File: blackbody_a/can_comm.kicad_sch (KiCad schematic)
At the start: 4 parts, among them J1 Conn_01x04_Pin, U1 TSL25911FN

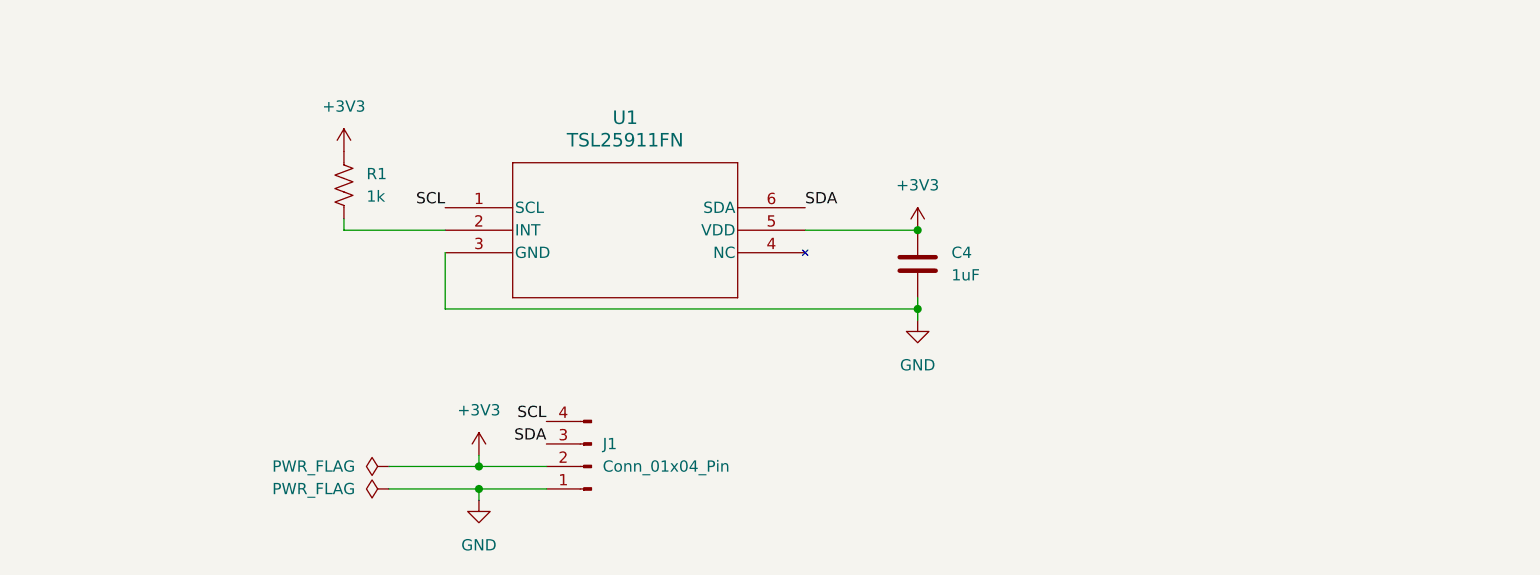
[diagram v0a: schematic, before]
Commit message: Added controller and CAN
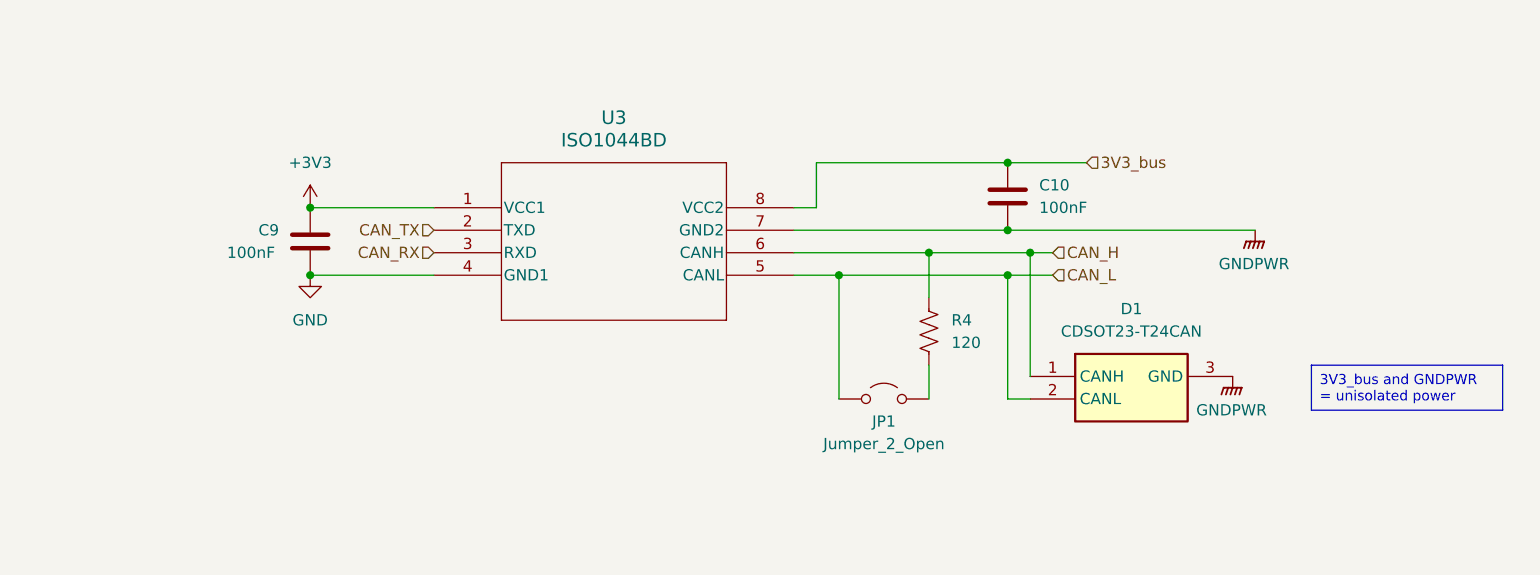
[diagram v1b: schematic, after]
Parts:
- removed C4: 1uF, symbol Device:C
- removed J1: Conn_01x04_Pin, symbol Connector:Conn_01x04_Pin
- removed R1: 1k, symbol Device:R_US
- removed U1: TSL25911FN, SON-06-FN_2000X2400_AMS, symbol TSL25911:TSL25911FN
- added C10, C9: 100nF, symbol Device:C
- added D1: CDSOT23-T24CAN, SOT95P230X117-3N, symbol CDSOT23-T24CAN:CDSOT23-T24CAN
- added JP1: Jumper_2_Open, symbol Jumper:Jumper_2_Open
- added R4: 120, symbol Device:R_US
- added U3: ISO1044BD, SOIC8_D_TEX, symbol ISO1044:ISO1044BD
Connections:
- net +3V3: now also C9.1, U3.1 (VCC1)
- net GND: now also C9.2, U3.4 (GND1)
- new net: JP1.2 (B), R4.2
- new net 3V3_bus: C10.1, U3.8 (VCC2)
- new net CAN_H: D1.1 (CANH), R4.1, U3.6 (CANH)
- new net CAN_L: D1.2 (CANL), JP1.1 (A), U3.5 (CANL)
- new net CAN_RX: U3.3 (RXD)
- new net CAN_TX: U3.2 (TXD)
- new net GNDPWR: C10.2, D1.3 (GND), U3.7 (GND2)

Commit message: Added power distribution
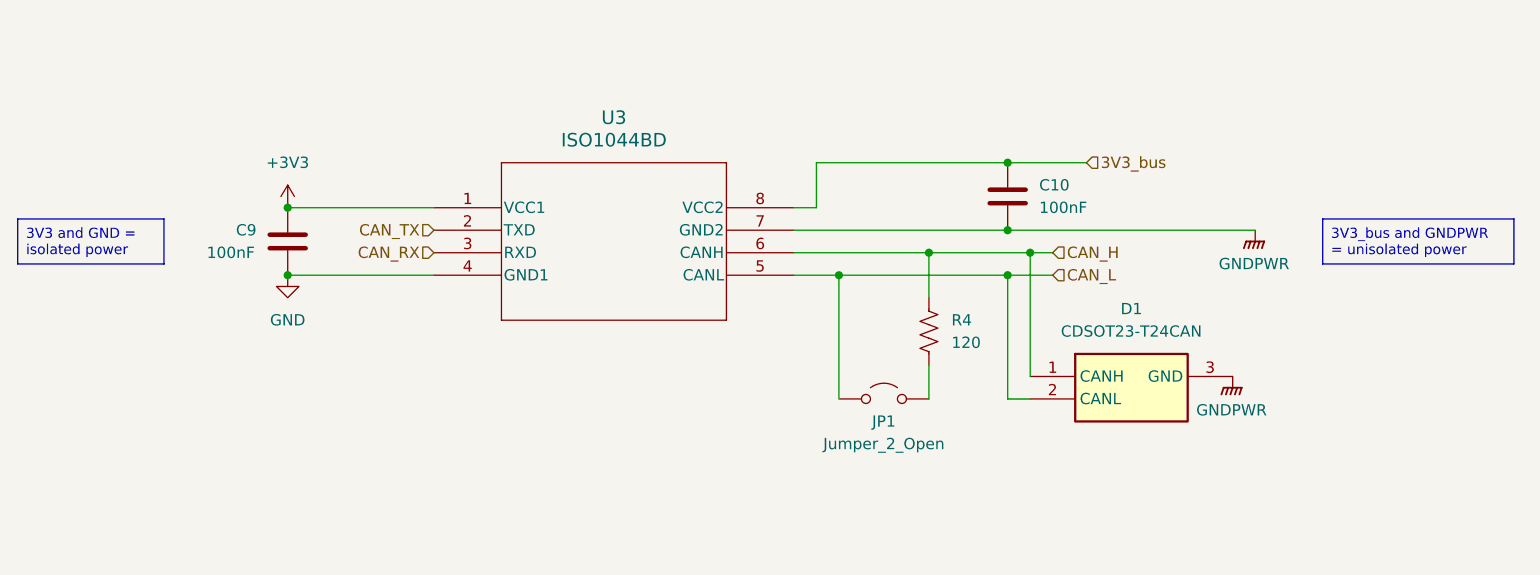
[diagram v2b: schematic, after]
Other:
- moved on the sheet: C9
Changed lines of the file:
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@@
 	(paper "A4")
 	(junction
-		(at 83.82 87.63)
+		(at 81.28 87.63)
 		(diameter 0)
 		(color 0 0 0 0)
@@
 	)
 	(junction
-		(at 83.82 95.25)
+		(at 81.28 95.25)
 		(diameter 0)
 		(color 0 0 0 0)
@@
 	(wire
 		(pts
-			(xy 83.82 95.25) (xy 97.79 95.25)
+			(xy 81.28 95.25) (xy 97.79 95.25)
 		)
 		(stroke
@@
 	(wire
 		(pts
-			(xy 97.79 87.63) (xy 83.82 87.63)
+			(xy 97.79 87.63) (xy 81.28 87.63)
 		)
 		(stroke
@@
 	(text_box "3V3_bus and GNDPWR = unisolated power"
 		(exclude_from_sim no)
-		(at 196.85 105.41 0)
+		(at 198.12 88.9 0)
 		(size 21.59 5.08)
+		(stroke
+			(width 0)
+			(type default)
+		)
+		(fill
+			(type none)
+		)
+		(effects
+			(font
+				(size 1.143 1.143)
+			)
+			(justify left top)
+		)
+	)
+	(text_box "3V3 and GND = isolated power"
+		(exclude_from_sim no)
+		(at 50.8 88.9 0)
+		(size 16.51 5.08)
 		(stroke
 			(width 0)
@@
 		)
 		(instances
-			(project ""
+			(project "blackbody_a"
 				(path "/1fc8ae43-742a-46b6-a93b-79253d0d0202/faa728f8-ddc6-4e3f-b104-4874b0828b62"
 					(reference "#PWR019")
@@
 		)
 		(instances
-			(project ""
+			(project "blackbody_a"
 				(path "/1fc8ae43-742a-46b6-a93b-79253d0d0202/faa728f8-ddc6-4e3f-b104-4874b0828b62"
 					(reference "JP1")
@@
 		)
 		(instances
-			(project ""
+			(project "blackbody_a"
 				(path "/1fc8ae43-742a-46b6-a93b-79253d0d0202/faa728f8-ddc6-4e3f-b104-4874b0828b62"
 					(reference "D1")
@@
 		)
 		(instances
-			(project ""
+			(project "blackbody_a"
 				(path "/1fc8ae43-742a-46b6-a93b-79253d0d0202/faa728f8-ddc6-4e3f-b104-4874b0828b62"
 					(reference "U3")
@@
 		)
 		(instances
-			(project ""
+			(project "blackbody_a"
 				(path "/1fc8ae43-742a-46b6-a93b-79253d0d0202/faa728f8-ddc6-4e3f-b104-4874b0828b62"
 					(reference "R4")
@@
 	(symbol
 		(lib_id "power:GND")
-		(at 83.82 95.25 0)
+		(at 81.28 95.25 0)
 		(unit 1)
 		(exclude_from_sim no)
@@
 		(fields_autoplaced yes)
 		(property "Reference" "#PWR018"
-			(at 83.82 101.6 0)
+			(at 81.28 101.6 0)
 			(effects
 				(font
@@
 		)
 		(property "Value" "GND"
-			(at 83.82 100.33 0)
+			(at 81.28 100.33 0)
 			(effects
 				(font
@@
 		)
 		(property "Footprint" ""
-			(at 83.82 95.25 0)
+			(at 81.28 95.25 0)
 			(effects
 				(font
@@
 		)
 		(property "Datasheet" ""
-			(at 83.82 95.25 0)
+			(at 81.28 95.25 0)
 			(effects
 				(font
@@
 		)
 		(property "Description" "Power symbol creates a global label with name \"GND\" , ground"
-			(at 83.82 95.25 0)
+			(at 81.28 95.25 0)
 			(effects
 				(font
@@
 		)
 		(instances
-			(project ""
+			(project "blackbody_a"
 				(path "/1fc8ae43-742a-46b6-a93b-79253d0d0202/faa728f8-ddc6-4e3f-b104-4874b0828b62"
 					(reference "#PWR018")
@@
 	(symbol
 		(lib_id "power:+3V3")
-		(at 83.82 87.63 0)
+		(at 81.28 87.63 0)
 		(unit 1)
 		(exclude_from_sim no)
@@
 		(fields_autoplaced yes)
 		(property "Reference" "#PWR017"
-			(at 83.82 91.44 0)
+			(at 81.28 91.44 0)
 			(effects
 				(font
@@
 		)
 		(property "Value" "+3V3"
-			(at 83.82 82.55 0)
+			(at 81.28 82.55 0)
 			(effects
 				(font
@@
 		)
 		(property "Footprint" ""
-			(at 83.82 87.63 0)
+			(at 81.28 87.63 0)
 			(effects
 				(font
@@
 		)
 		(property "Datasheet" ""
-			(at 83.82 87.63 0)
+			(at 81.28 87.63 0)
 			(effects
 				(font
@@
 		)
 		(property "Description" "Power symbol creates a global label with name \"+3V3\""
-			(at 83.82 87.63 0)
+			(at 81.28 87.63 0)
 			(effects
 				(font
@@
 		)
 		(instances
-			(project ""
+			(project "blackbody_a"
 				(path "/1fc8ae43-742a-46b6-a93b-79253d0d0202/faa728f8-ddc6-4e3f-b104-4874b0828b62"
 					(reference "#PWR017")
@@
 	(symbol
 		(lib_id "Device:C")
-		(at 83.82 91.44 0)
+		(at 81.28 91.44 0)
 		(unit 1)
 		(exclude_from_sim no)
@@
 		(dnp no)
 		(property "Reference" "C9"
-			(at 77.978 90.17 0)
+			(at 75.438 90.17 0)
 			(effects
 				(font
@@
 		)
 		(property "Value" "100nF"
-			(at 74.422 92.71 0)
+			(at 72.136 92.71 0)
 			(effects
 				(font
@@
 		)
 		(property "Footprint" ""
-			(at 84.7852 95.25 0)
+			(at 82.2452 95.25 0)
 			(effects
 				(font
@@
 		)
 		(property "Datasheet" "~"
-			(at 83.82 91.44 0)
+			(at 81.28 91.44 0)
 			(effects
 				(font
@@
 		)
 		(property "Description" "Unpolarized capacitor"
-			(at 83.82 91.44 0)
+			(at 81.28 91.44 0)
 			(effects
 				(font
@@
 		)
 		(instances
-			(project ""
+			(project "blackbody_a"
 				(path "/1fc8ae43-742a-46b6-a93b-79253d0d0202/faa728f8-ddc6-4e3f-b104-4874b0828b62"
 					(reference "C9")

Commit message: Fixed pins, minor changes, removed power isolation
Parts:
- removed C10: 100nF, symbol Device:C
- removed U3: ISO1044BD, SOIC8_D_TEX, symbol ISO1044:ISO1044BD
- added D7: CAN_LED, LED_SMD:LED_0805_2012Metric, symbol Device:LED
- added R18: 2.2k, Resistor_SMD:R_0805_2012Metric, symbol Device:R
- added U2: TCAN337DCNR, TCAN337DCNR:SOT65P280X145-8N, symbol TCAN337DCNR:TCAN337DCNR
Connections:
- net GNDPWR is gone; now on net GND: D1.3 (GND)
- net +3V3: now also R18.1, U2.2 (GND)
- net CAN_H: now also D1.2 (CANL), JP1.1 (A), U2.7 (CANH); no longer D1.1 (CANH), R4.1
- net CAN_L: now also D1.1 (CANH), R4.1, U2.6 (CANL); no longer D1.2 (CANL), JP1.1 (A)
- net CAN_RX: now also U2.4 (RXD)
- net CAN_TX: now also U2.1 (TXD)
- net GND: now also D7.1 (K), U2.3 (VCC)
- new net Fault: D7.2 (A), R18.2, U2.5 (FAULT)
- no-connect marks 0 -> 1
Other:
- moved on the sheet: D1, JP1, R4

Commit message: review changes
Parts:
- added R16: 10k, symbol Device:R_US
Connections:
- net Fault: now also R16.1; no longer D7.2 (A)
- new net: D7.2 (A), R16.2
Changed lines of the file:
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@@
+	(wire
+		(pts
+			(xy 191.77 78.74) (xy 191.77 80.01)
+		)
+		(stroke
+			(width 0)
+			(type default)
+		)
+	)
 	(wire
 		(pts
@@
 	(wire
 		(pts
+			(xy 191.77 68.58) (xy 191.77 71.12)
+		)
+		(stroke
+			(width 0)
+			(type default)
+		)
+	)
+	(wire
+		(pts
 			(xy 140.97 90.17) (xy 152.4 90.17)
 		)
@@
 		(pts
 			(xy 87.63 95.25) (xy 81.28 95.25)
-		)
-		(stroke
-			(width 0)
-			(type default)
-		)
-	)
-	(wire
-		(pts
-			(xy 191.77 74.93) (xy 191.77 80.01)
 		)
 		(stroke
@@
 	)
 	(label "Fault"
-		(at 191.77 74.93 0)
+		(at 191.77 68.58 0)
 		(fields_autoplaced yes)
 		(effects
@@
 					(unit 1)
 				)
+			)
+		)
+	)
+	(symbol
+		(lib_id "Device:R_US")
+		(at 191.77 74.93 0)
+		(unit 1)
+		(exclude_from_sim no)
+		(in_bom yes)
+		(on_board yes)
+		(dnp no)
+		(property "Reference" "R16"
+			(at 186.944 73.66 0)
+			(effects
+				(font
+					(size 1.27 1.27)
+				)
+				(justify left)
+			)
+		)
+		(property "Value" "10k"
+			(at 185.928 76.2 0)
+			(effects
+				(font
+					(size 1.27 1.27)
+				)
+				(justify left)
+			)
+		)
+		(property "Footprint" ""
+			(at 192.786 75.184 90)
+			(effects
+				(font
+					(size 1.27 1.27)
+				)
+				(hide yes)
+			)
+		)
+		(property "Datasheet" "~"
+			(at 191.77 74.93 0)
+			(effects
+				(font
+					(size 1.27 1.27)
+				)
+				(hide yes)
+			)
+		)
+		(property "Description" "Resistor, US symbol"
+			(at 191.77 74.93 0)
+			(effects
+				(font
+					(size 1.27 1.27)
+				)
+				(hide yes)
+			)
+		)
+		(pin "2"
+		)
+		(pin "1"
+		)
+		(instances
+			(project "blackbody_a"
+				(path "/1fc8ae43-742a-46b6-a93b-79253d0d0202/faa728f8-ddc6-4e3f-b104-4874b0828b62"
+					(reference "R16")
+					(unit 1)
+				)

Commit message: layout iteration 1
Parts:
- C9: footprint (none) -> Capacitor_SMD:C_0805_2012Metric
- D1: footprint SOT95P230X117-3N -> blackbody_a:SOT95P230X117-3N
- JP1: footprint (none) -> Connector_PinHeader_2.54mm:PinHeader_1x02_P2.54mm_Vertical
- R16, R4: footprint (none) -> Resistor_SMD:R_0805_2012Metric
- U2: footprint TCAN337DCNR:SOT65P280X145-8N -> UTSVT_ICs:SOP65P640X120-16N
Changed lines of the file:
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@@
 (kicad_sch
-	(version 20231120)
+	(version 20250114)
 	(generator "eeschema")
-	(generator_version "8.0")
+	(generator_version "9.0")
 	(paper "A4")
 	(junction
@@
 	(label "Fault"
 		(at 138.43 87.63 0)
-		(fields_autoplaced yes)
 		(effects
 			(font
@@
 	(label "Fault"
 		(at 191.77 68.58 0)
-		(fields_autoplaced yes)
 		(effects
 			(font
@@
 		(shape input)
 		(at 100.33 87.63 180)
-		(fields_autoplaced yes)
 		(effects
 			(font
@@
 		(shape input)
 		(at 154.94 92.71 0)
-		(fields_autoplaced yes)
 		(effects
 			(font
@@
 		(shape input)
 		(at 154.94 90.17 0)
-		(fields_autoplaced yes)
 		(effects
 			(font
@@
 		(shape input)
 		(at 100.33 95.25 180)
-		(fields_autoplaced yes)
 		(effects
 			(font
@@
 			)
 		)
-		(property "Footprint" ""
+		(property "Footprint" "Resistor_SMD:R_0805_2012Metric"
 			(at 192.786 75.184 90)
 			(effects
@@
 			)
 		)
-		(property "Footprint" ""
+		(property "Footprint" "Connector_PinHeader_2.54mm:PinHeader_1x02_P2.54mm_Vertical"
 			(at 135.89 106.68 0)
 			(effects
@@
 			)
 		)
-		(property "Footprint" "SOT95P230X117-3N"
+		(property "Footprint" "blackbody_a:SOT95P230X117-3N"
 			(at 171.45 199.06 0)
 			(effects
@@
 			)
 		)
-		(property "Footprint" ""
+		(property "Footprint" "Resistor_SMD:R_0805_2012Metric"
 			(at 141.986 99.314 90)
 			(effects
@@
 			)
 		)
-		(property "Footprint" "TCAN337DCNR:SOT65P280X145-8N"
+		(property "Footprint" "UTSVT_ICs:SOP65P640X120-16N"
 			(at 115.57 95.25 0)
 			(effects
@@
 			)
 		)
-		(property "Footprint" ""
+		(property "Footprint" "Capacitor_SMD:C_0805_2012Metric"
 			(at 82.2452 95.25 0)
 			(effects

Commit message: layout edits
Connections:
- net +3V3 renamed +3.3V
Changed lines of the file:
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@@
-	)
-	(junction
-		(at 81.28 87.63)
-		(diameter 0)
-		(color 0 0 0 0)
 	)
 	(junction
@@
 	(junction
 		(at 81.28 95.25)
+		(diameter 0)
+		(color 0 0 0 0)
+	)
+	(junction
+		(at 81.28 87.63)
 		(diameter 0)
 		(color 0 0 0 0)
@@
 			)
 			(justify right)
-		)
-	)
-	(symbol
-		(lib_id "power:+3V3")
-		(at 132.08 77.47 0)
-		(unit 1)
-		(exclude_from_sim no)
-		(in_bom yes)
-		(on_board yes)
-		(dnp no)
-		(fields_autoplaced yes)
-		(property "Reference" "#PWR010"
-			(at 132.08 81.28 0)
-			(effects
-				(font
-					(size 1.27 1.27)
-				)
-				(hide yes)
-			)
-		)
-		(property "Value" "+3V3"
-			(at 132.08 72.39 0)
-			(effects
-				(font
-					(size 1.27 1.27)
-				)
-			)
-		)
-		(property "Footprint" ""
-			(at 132.08 77.47 0)
-			(effects
-				(font
-					(size 1.27 1.27)
-				)
-				(hide yes)
-			)
-		)
-		(property "Datasheet" ""
-			(at 132.08 77.47 0)
-			(effects
-				(font
-					(size 1.27 1.27)
-				)
-				(hide yes)
-			)
-		)
-		(property "Description" "Power symbol creates a global label with name \"+3V3\""
-			(at 132.08 77.47 0)
-			(effects
-				(font
-					(size 1.27 1.27)
-				)
-				(hide yes)
-			)
-		)
-		(pin "1"
-		)
-		(instances
-			(project "blackbody_a"
-				(path "/1fc8ae43-742a-46b6-a93b-79253d0d0202/faa728f8-ddc6-4e3f-b104-4874b0828b62"
-					(reference "#PWR010")
-					(unit 1)
-				)
-			)
 		)
 	)
@@
 	)
 	(symbol
+		(lib_id "power:+3.3V")
+		(at 81.28 87.63 0)
+		(unit 1)
+		(exclude_from_sim no)
+		(in_bom yes)
+		(on_board yes)
+		(dnp no)
+		(fields_autoplaced yes)
+		(property "Reference" "#PWR017"
+			(at 81.28 91.44 0)
+			(effects
+				(font
+					(size 1.27 1.27)
+				)
+				(hide yes)
+			)
+		)
+		(property "Value" "+3.3V"
+			(at 81.28 82.55 0)
+			(effects
+				(font
+					(size 1.27 1.27)
+				)
+			)
+		)
+		(property "Footprint" ""
+			(at 81.28 87.63 0)
+			(effects
+				(font
+					(size 1.27 1.27)
+				)
+				(hide yes)
+			)
+		)
+		(property "Datasheet" ""
+			(at 81.28 87.63 0)
+			(effects
+				(font
+					(size 1.27 1.27)
+				)
+				(hide yes)
+			)
+		)
+		(property "Description" "Power symbol creates a global label with name \"+3.3V\""
+			(at 81.28 87.63 0)
+			(effects
+				(font
+					(size 1.27 1.27)
+				)
+				(hide yes)
+			)
+		)
+		(pin "1"
+		)
+		(instances
+			(project "blackbody_a"
+				(path "/1fc8ae43-742a-46b6-a93b-79253d0d0202/faa728f8-ddc6-4e3f-b104-4874b0828b62"
+					(reference "#PWR017")
+					(unit 1)
+				)
+			)
+		)
+	)
+	(symbol
+		(lib_id "power:+3.3V")
+		(at 132.08 77.47 0)
+		(unit 1)
+		(exclude_from_sim no)
+		(in_bom yes)
+		(on_board yes)
+		(dnp no)
+		(fields_autoplaced yes)
+		(property "Reference" "#PWR010"
+			(at 132.08 81.28 0)
+			(effects
+				(font
+					(size 1.27 1.27)
+				)
+				(hide yes)
+			)
+		)
+		(property "Value" "+3.3V"
+			(at 132.08 72.39 0)
+			(effects
+				(font
+					(size 1.27 1.27)
+				)
+			)
+		)
+		(property "Footprint" ""
+			(at 132.08 77.47 0)
+			(effects
+				(font
+					(size 1.27 1.27)
+				)
+				(hide yes)
+			)
+		)
+		(property "Datasheet" ""
+			(at 132.08 77.47 0)
+			(effects
+				(font
+					(size 1.27 1.27)
+				)
+				(hide yes)
+			)
+		)
+		(property "Description" "Power symbol creates a global label with name \"+3.3V\""
+			(at 132.08 77.47 0)
+			(effects
+				(font
+					(size 1.27 1.27)
+				)
+				(hide yes)
+			)
+		)
+		(pin "1"
+		)
+		(instances
+			(project ""
+				(path "/1fc8ae43-742a-46b6-a93b-79253d0d0202/faa728f8-ddc6-4e3f-b104-4874b0828b62"
+					(reference "#PWR010")
+					(unit 1)
+				)
+			)
+		)
+	)
+	(symbol
 		(lib_id "power:GND")
 		(at 175.26 104.14 0)
@@
 					(unit 1)
 				)
-			)
-		)
-	)
-	(symbol
-		(lib_id "power:+3V3")
-		(at 81.28 87.63 0)
-		(unit 1)
-		(exclude_from_sim no)
-		(in_bom yes)
-		(on_board yes)
-		(dnp no)
-		(fields_autoplaced yes)
-		(property "Reference" "#PWR017"
-			(at 81.28 91.44 0)
-			(effects
-				(font
-					(size 1.27 1.27)
-				)
-				(hide yes)
-			)
-		)
-		(property "Value" "+3V3"
-			(at 81.28 82.55 0)
-			(effects
-				(font
-					(size 1.27 1.27)
-				)
-			)
-		)
-		(property "Footprint" ""
-			(at 81.28 87.63 0)
-			(effects
-				(font
-					(size 1.27 1.27)
-				)
-				(hide yes)
-			)
-		)
-		(property "Datasheet" ""
-			(at 81.28 87.63 0)
-			(effects
-				(font
-					(size 1.27 1.27)
-				)
-				(hide yes)
-			)
-		)
-		(property "Description" "Power symbol creates a global label with name \"+3V3\""
-			(at 81.28 87.63 0)
-			(effects
-				(font
-					(size 1.27 1.27)
-				)
-				(hide yes)
-			)
-		)
-		(pin "1"
-		)
-		(instances
-			(project "blackbody_a"
-				(path "/1fc8ae43-742a-46b6-a93b-79253d0d0202/faa728f8-ddc6-4e3f-b104-4874b0828b62"
-					(reference "#PWR017")
-					(unit 1)
-				)
